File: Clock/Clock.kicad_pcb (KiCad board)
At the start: 2 copper layers, 72.4 x 63.5 mm, 39 parts, among them J1 Power, J2 Signal, SW1 SW_Push, SW2 SW_DPDT_x2, U1 74LS04, U2 LM555, U3 74LS08, U4 74LS32, U5 LM555, U6 LM555

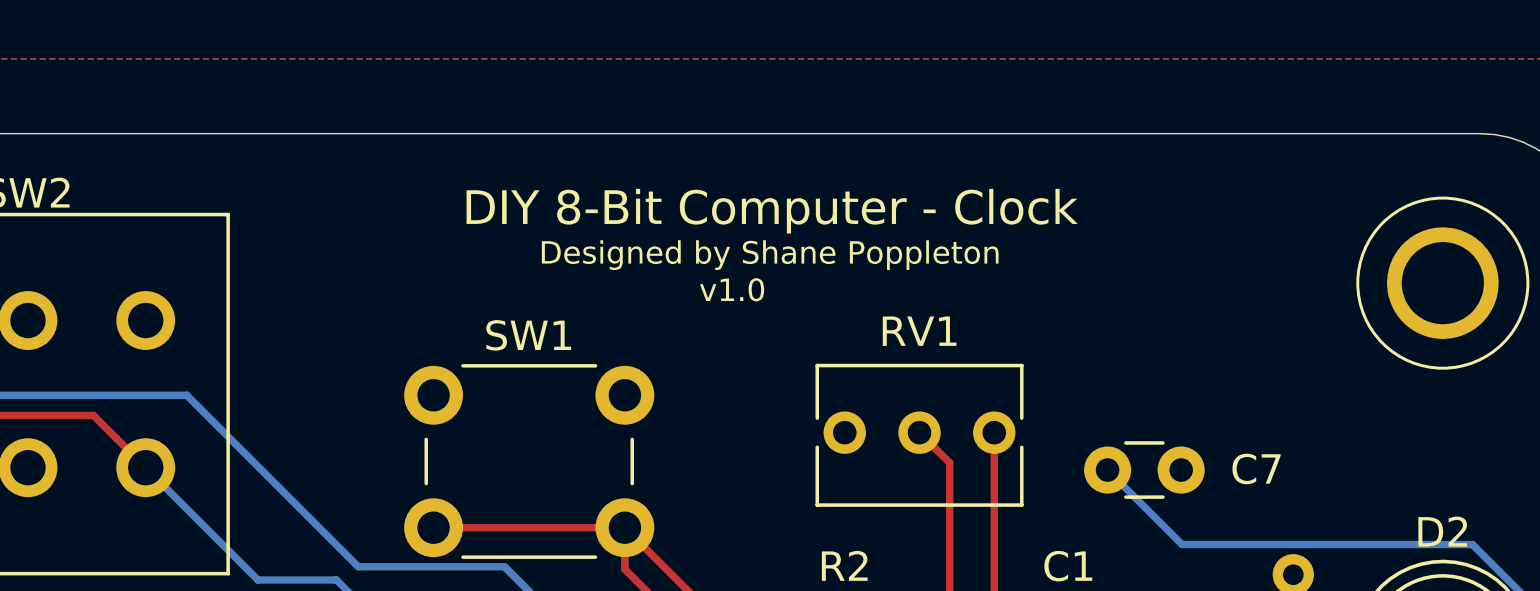
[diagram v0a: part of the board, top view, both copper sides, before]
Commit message: Clock: Added attributions, re-plotted gerbers
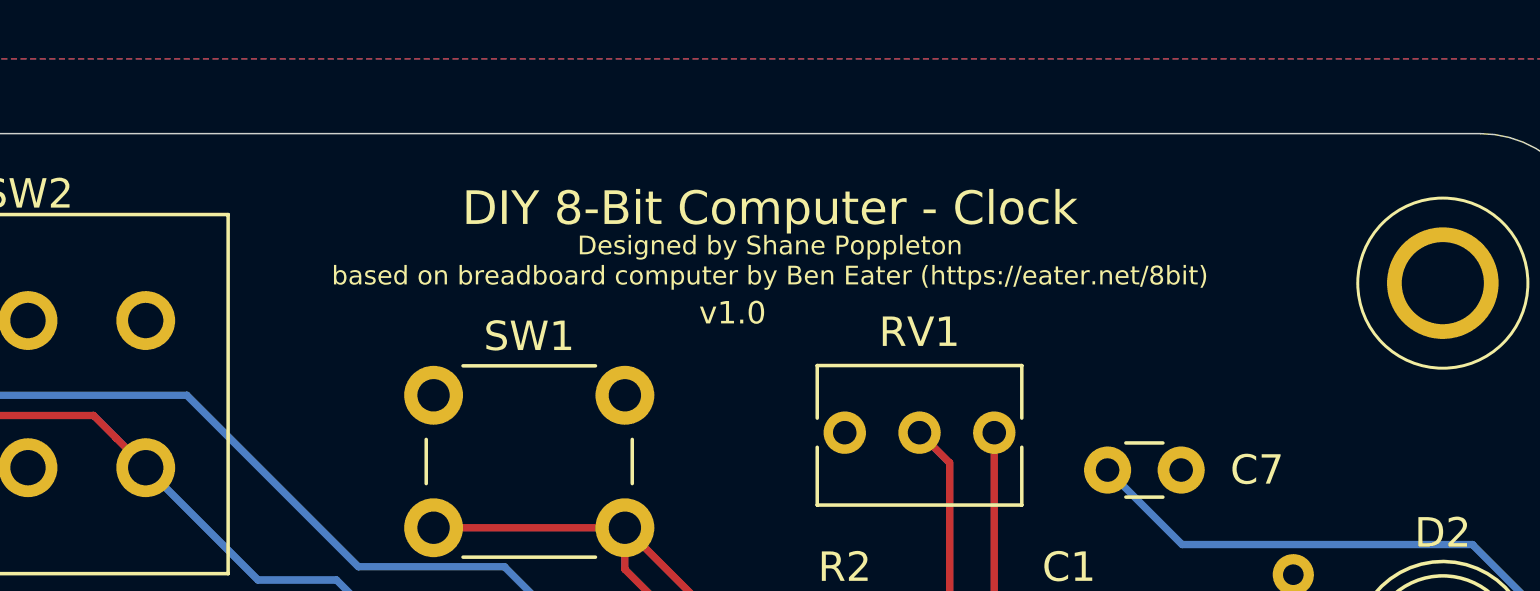
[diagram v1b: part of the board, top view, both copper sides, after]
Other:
- board text added: "Designed by Shane Poppleton based on breadboard computer by Ben Eater (https://eater.net/8bit)"
- board text removed: "Designed by Shane Poppleton"
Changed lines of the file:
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@@
     (title "DIY 8-Bit Computer - Clock")
     (rev v01)
-    (comment 2 creativecommons.org/licenses/by/4.0)
-    (comment 3 "License CC by 4.0")
+    (comment 1 creativecommons.org/licenses/by/4.0)
+    (comment 2 "License CC by 4.0")
+    (comment 3 "Based on breadboard computer by Ben Eater")
     (comment 4 "Author: Shane Poppleton")
   )
@@
     )
   )
-  (gr_text "v1.0\n" (at 154.432 65.024) (layer F.SilkS)
+  (gr_text "v1.0\n" (at 154.432 65.786) (layer F.SilkS)
     (effects (font (size 0.762 0.762) (thickness 0.127)))
   )
-  (gr_text "Designed by Shane Poppleton\n" (at 155.702 63.754) (layer F.SilkS)
-    (effects (font (size 0.762 0.762) (thickness 0.127)))
+  (gr_text "Designed by Shane Poppleton\nbased on breadboard computer by Ben Eater (https://eater.net/8bit)\n" (at 155.702 64.008) (layer F.SilkS)
+    (effects (font (size 0.635 0.635) (thickness 0.1016)))
   )
   (gr_text "DIY 8-Bit Computer - Clock" (at 155.702 62.23) (layer F.SilkS)
